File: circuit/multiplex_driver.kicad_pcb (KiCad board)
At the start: 2 copper layers, 46 parts, among them P1 Keypad, P2 I2C, P3 +5V, P4 Anodes, P5 Cathode 1-8, P6 Cathode 9-16, P7 Serial, P8 +24V, Q1 BC546A, Q2 BC546A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

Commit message: Added pins for pr28v
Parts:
- added P9: pr28v, PIN_ARRAY_4x1, F.Cu at (32.8, 25.5)
- moved P8 11.4 mm to (34.0, 34.6), turned to 180 degrees
- moved P1 2.40 mm to (140.3, 58.6)
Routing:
- net M-RCLK: track 90.7 -> 109.0 mm
- net K-SER: track 82.3 -> 99.8 mm
- net N-0000022: track 21.1 -> 34.8 mm
- net N-0000020: track 27.5 -> 38.1 mm
- net N-0000026: track 38.9 -> 28.3 mm
- net N-0000094: track 24.8 -> 31.2 mm
- net N-0000092: track 26.0 -> 32.2 mm
- net MOTOR+: track 39.8 -> 45.0 mm
- net N-0000042: track 19.9 -> 24.9 mm
- net M-SRCLK: track 101.0 -> 105.3 mm
- net GND: track 327.8 -> 332.0 mm
- net N-0000028: track 25.7 -> 21.9 mm, vias 0 -> 1
- net N-0000044: track 25.3 -> 21.8 mm
- net N-0000043: track 23.3 -> 26.8 mm
- net N-0000019: track 23.8 -> 20.5 mm
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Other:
- board outline added: 133 x 53.9 mm
- board text added: "Vending Machine Driver - v1.0 Designed by: John Spencer & Tim Crawley, 2015 https://github.com/CCHS-Melbourne/VendDrv Made at hackmelbourne.org"

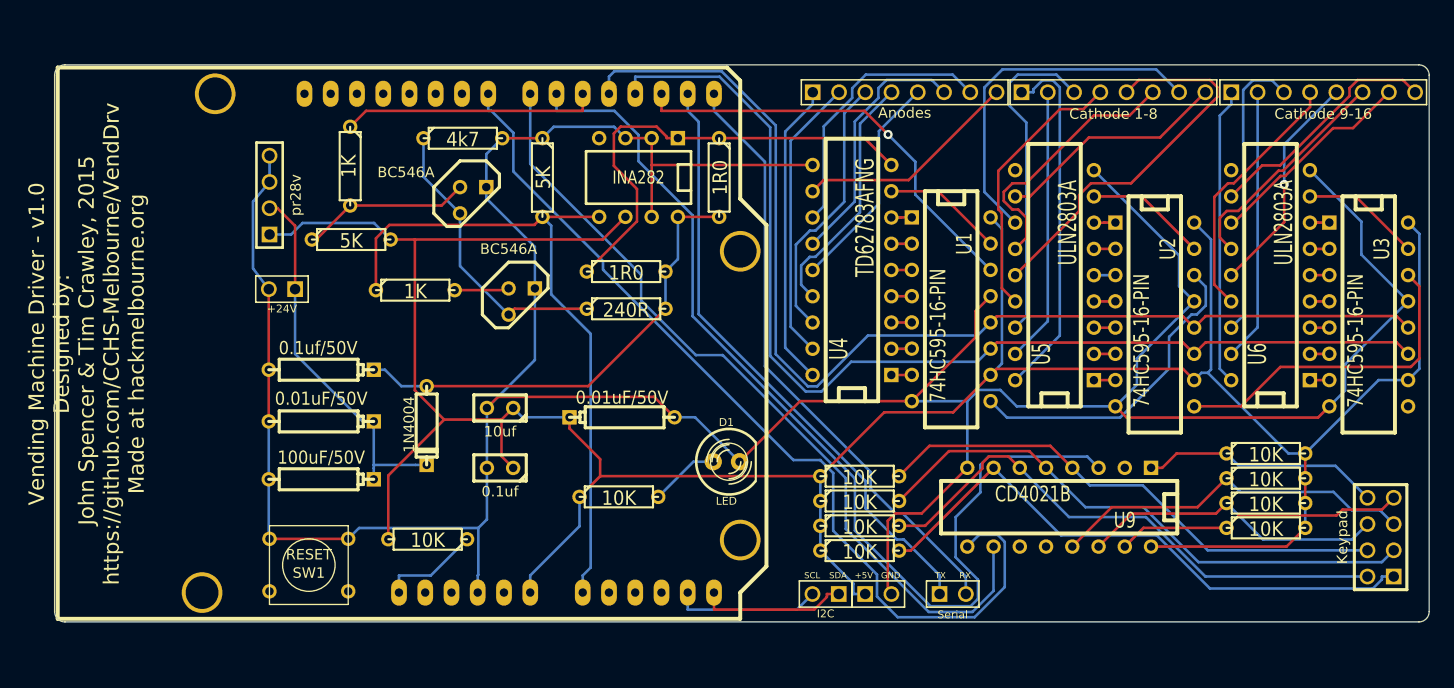
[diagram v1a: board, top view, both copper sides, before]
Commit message: Updated for better 24v section.
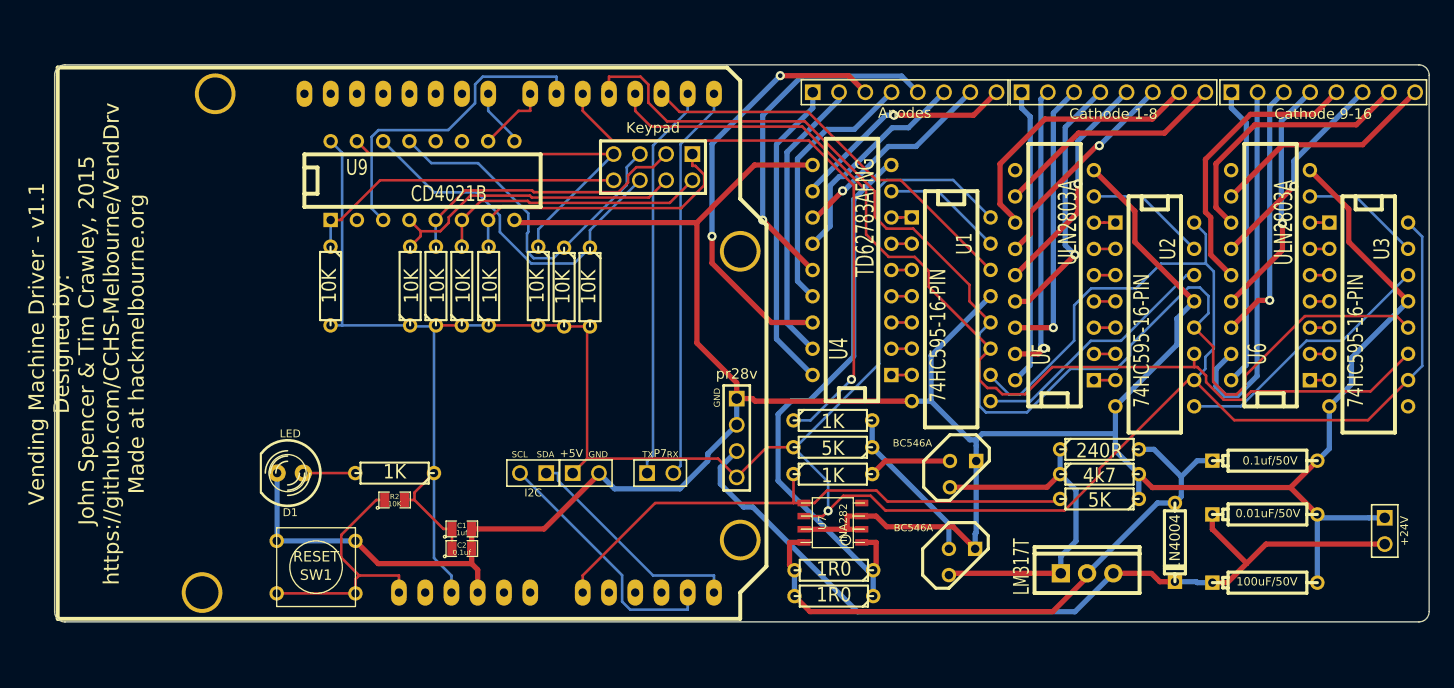
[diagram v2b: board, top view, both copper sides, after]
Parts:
- removed C6: 0.01uF/50V, CP4
- added U8: LM317T, LM317T, F.Cu at (111.9, 62.1)
- C1: value 10uf -> 1uf; footprint C1 -> SM0805
- C2: footprint C1 -> SM0805
- R1: value 10K -> 1K
- R2: footprint R3 -> SM0805
- U7: footprint DIP-8__300 -> so-8
- moved P8 109.2 mm to (140.7, 58.0), turned to 270 degrees
- moved R14 91.9 mm to (38.7, 34.3), turned to 270 degrees
- moved C3 91.8 mm to (129.1, 63.0), turned to 0 degrees
- moved C4 91.7 mm to (129.1, 56.4), turned to 0 degrees
- moved C5 91.7 mm to (129.1, 51.2), turned to 0 degrees
- moved P1 79.0 mm to (69.9, 22.8), turned to 180 degrees
- moved R15 74.2 mm to (58.8, 34.3), turned to 270 degrees
- moved D2 73.3 mm to (120.4, 59.1)
- moved R17 70.4 mm to (61.3, 34.4), turned to 270 degrees
- moved R5 69.6 mm to (113.1, 52.5)
- moved U9 69.2 mm to (47.6, 24.1), turned to 0 degrees
- moved R16 68.7 mm to (63.8, 34.4), turned to 270 degrees
- moved R4 62.2 mm to (113.1, 54.9), turned to 180 degrees
- moved Q1 58.8 mm to (99.8, 61.0)
- moved R3 52.8 mm to (87.3, 47.3), turned to 0 degrees
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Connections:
- P8 pad 1: +24V -> GND
- P8 pad 2: GND -> +24V
- P9 pad 1: +5V -> GND
- P9 pad 2: +24V -> GND
- P9 pad 3: GND -> +24V
- P9 pad 4: GND -> +5V
- R2 pad 1: N-0000015 (its old number) -> N-0000094
- SHIELD1 pad 5V: (no net) -> +5V
- SHIELD1 pad RST: N-0000015 (its old number) -> N-0000094
- SHIELD1 pad V_IN: +5V -> (no net)
- SW1 pad 1: (no net) -> N-0000094
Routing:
- net K-RCLK: track 89.1 -> 5.64 mm
- net K-SRCLK: track 79.0 -> 6.94 mm
- net K-SER: track 99.8 -> 31.5 mm
- net +24V: track 36.6 -> 82.8 mm
- net M-ON/OFF: track 24.8 -> 57.0 mm, vias 0 -> 1
- net N-0000058: track 56.7 -> 28.7 mm
- net N-0000081: track 54.8 -> 28.1 mm
- net N-0000082: track 53.2 -> 26.6 mm
- net N-0000094: track 0.00 -> 25.3 mm
- net GND: track 332.0 -> 310.2 mm
- net N-0000080: track 50.7 -> 29.7 mm
- net N-0000066: track 58.9 -> 38.3 mm
- net N-0000065: track 58.9 -> 38.3 mm
- net N-0000044: track 38.1 -> 22.2 mm, vias 0 -> 1
- net N-0000035: track 26.0 -> 41.9 mm, vias 0 -> 2
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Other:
- net class Heavy added: clearance 0.508, trace_width 0.508, via_dia 0.889, via_drill 0.635
- board text added: "Vending Machine Driver - v1.1 Designed by: John Spencer & Tim Crawley, 2015 https://github.com/CCHS-Melbourne/VendDrv Made at hackmelbourne.org"
- board text removed: "Vending Machine Driver - v1.0 Designed by: John Spencer & Tim Crawley, 2015 https://github.com/CCHS-Melbourne/VendDrv Made at hackmelbourne.org"
